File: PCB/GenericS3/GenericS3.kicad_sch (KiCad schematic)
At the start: 69 parts, among them J1 USB-C, J2 Shelly, J5 POWER, P1 33, P10 42, P11 45, P12 46, P13 47, P14 48, P15 18, P16 19, P17 14, P18 15, P19 16, P2 34, P20 17, P21 6, P22 7, P23 8, P24 9, P25 20, P26 10, P27 11, P28 12, P29 13, P3 35, P30 1, P31 2, P32 3, P33 4, P34 5, P35 21, P36 43, P37 44, P38 0, P39 ⏚, P4 36, P40 ⏚, P41 ⏚, P42 ⏚, P43 +, P44 +, P45 +, P46 +, P5 37, P6 38, P7 39, P8 40, P9 41, U1 Barcode, U2 ESP32-S3-MINI-1, U5 MD8942

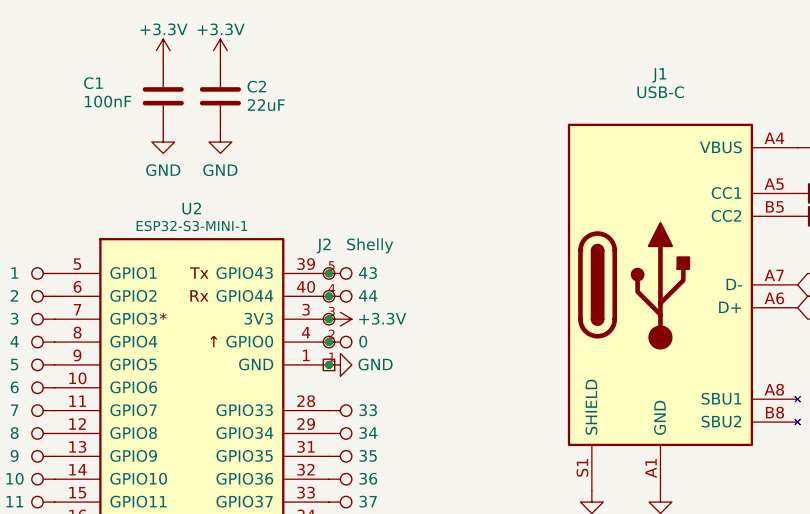
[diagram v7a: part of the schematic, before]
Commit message: PROG under ESP
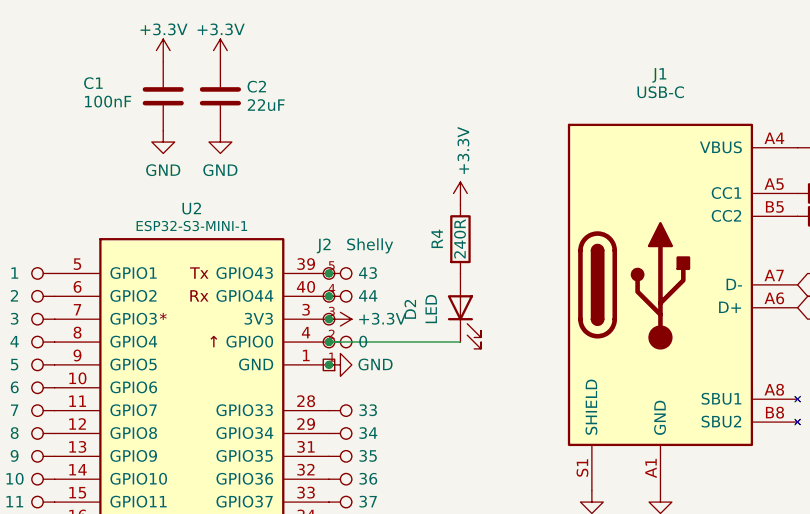
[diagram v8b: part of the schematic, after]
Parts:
- added D2: LED, LED_SMD:LED_0402_1005Metric, symbol Device:LED
- added R4: 240R, RevK:R_0402, symbol Device:R
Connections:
- net +3.3V: now also R4.1
- net at J2.2 (0), P38.1 (P), U2.4 (GPIO0): now also D2.1 (K)
- new net: D2.2 (A), R4.2
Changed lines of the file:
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@@
+    (stroke (width 0) (type default))
+  )
+  (wire (pts (xy 124.46 60.325) (xy 139.065 60.325))
     (stroke (width 0) (type default))
   )
@@
     )
   )
+  (symbol (lib_id "Device:LED") (at 139.065 56.515 90) (unit 1)
+    (in_bom yes) (on_board yes) (dnp no)
+    (property "Reference" "D2" (at 133.5532 56.6928 0)
+      (effects (font (size 1.27 1.27)))
+    )
+    (property "Value" "LED" (at 135.8646 56.6928 0)
+      (effects (font (size 1.27 1.27)))
+    )
+    (property "Footprint" "LED_SMD:LED_0402_1005Metric" (at 139.065 56.515 0)
+      (effects (font (size 1.27 1.27)) hide)
+    )
+    (property "Datasheet" "~" (at 139.065 56.515 0)
+      (effects (font (size 1.27 1.27)) hide)
+    )
+    (property "LCSC Part #" "C965790" (at 139.065 56.515 0)
+      (effects (font (size 1.27 1.27)) hide)
+    )
+    (pin "1")
+    (pin "2")
+    (instances
+      (project "GenericS3"
+        (path "/2d210a96-f81f-42a9-8bf4-1b43c11086f3"
+          (reference "D2") (unit 1)
+        )
+      )
+      (project "Tas"
+        (path "/42713045-fffd-4b2d-ae1e-7232d705fb12"
+          (reference "D3") (unit 1)
+        )
+      )
+    )
+  )
   (symbol (lib_id "power:+3.3V") (at 138.43 99.695 0) (unit 1)
     (in_bom yes) (on_board yes) (dnp no) (fields_autoplaced)
@@
     )
   )
+  (symbol (lib_id "power:+3.3V") (at 139.065 45.085 0) (unit 1)
+    (in_bom yes) (on_board yes) (dnp no)
+    (property "Reference" "#PWR022" (at 139.065 48.895 0)
+      (effects (font (size 1.27 1.27)) hide)
+    )
+    (property "Value" "+3.3V" (at 139.446 41.8338 90)
+      (effects (font (size 1.27 1.27)) (justify left))
+    )
+    (property "Footprint" "" (at 139.065 45.085 0)
+      (effects (font (size 1.27 1.27)) hide)
+    )
+    (property "Datasheet" "" (at 139.065 45.085 0)
+      (effects (font (size 1.27 1.27)) hide)
+    )
+    (pin "1")
+    (instances
+      (project "GenericS3"
+        (path "/2d210a96-f81f-42a9-8bf4-1b43c11086f3"
+          (reference "#PWR022") (unit 1)
+        )
+      )
+      (project "Tas"
+        (path "/42713045-fffd-4b2d-ae1e-7232d705fb12"
+          (reference "#PWR021") (unit 1)
+        )
+      )
+    )
+  )
   (symbol (lib_id "power:+3.3V") (at 112.395 29.21 0) (unit 1)
     (in_bom yes) (on_board yes) (dnp no) (fields_autoplaced)
@@
         )
       )
+    )
+  )
+  (symbol (lib_id "Device:R") (at 139.065 48.895 0) (unit 1)
+    (in_bom yes) (on_board yes) (dnp no)
+    (property "Reference" "R4" (at 136.525 48.895 90)
+      (effects (font (size 1.27 1.27)))
+    )
+    (property "Value" "240R" (at 139.065 48.895 90)
+      (effects (font (size 1.27 1.27)))
+    )
+    (property "Footprint" "RevK:R_0402" (at 137.287 48.895 90)
+      (effects (font (size 1.27 1.27)) hide)
+    )
+    (property "Datasheet" "~" (at 139.065 48.895 0)
+      (effects (font (size 1.27 1.27)) hide)
+    )
+    (pin "1")
+    (pin "2")
+    (instances
+      (project "GenericS3"
+        (path "/2d210a96-f81f-42a9-8bf4-1b43c11086f3"
+          (reference "R4") (unit 1)
+        )
+      )
+      (project "Tas"
+        (path "/42713045-fffd-4b2d-ae1e-7232d705fb12"
+          (reference "R5") (unit 1)
+        )
+      )
